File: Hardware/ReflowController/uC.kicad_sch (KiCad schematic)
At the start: 33 parts, among them J13 Conn_01x15_Female, J14 Conn_01x15_Female

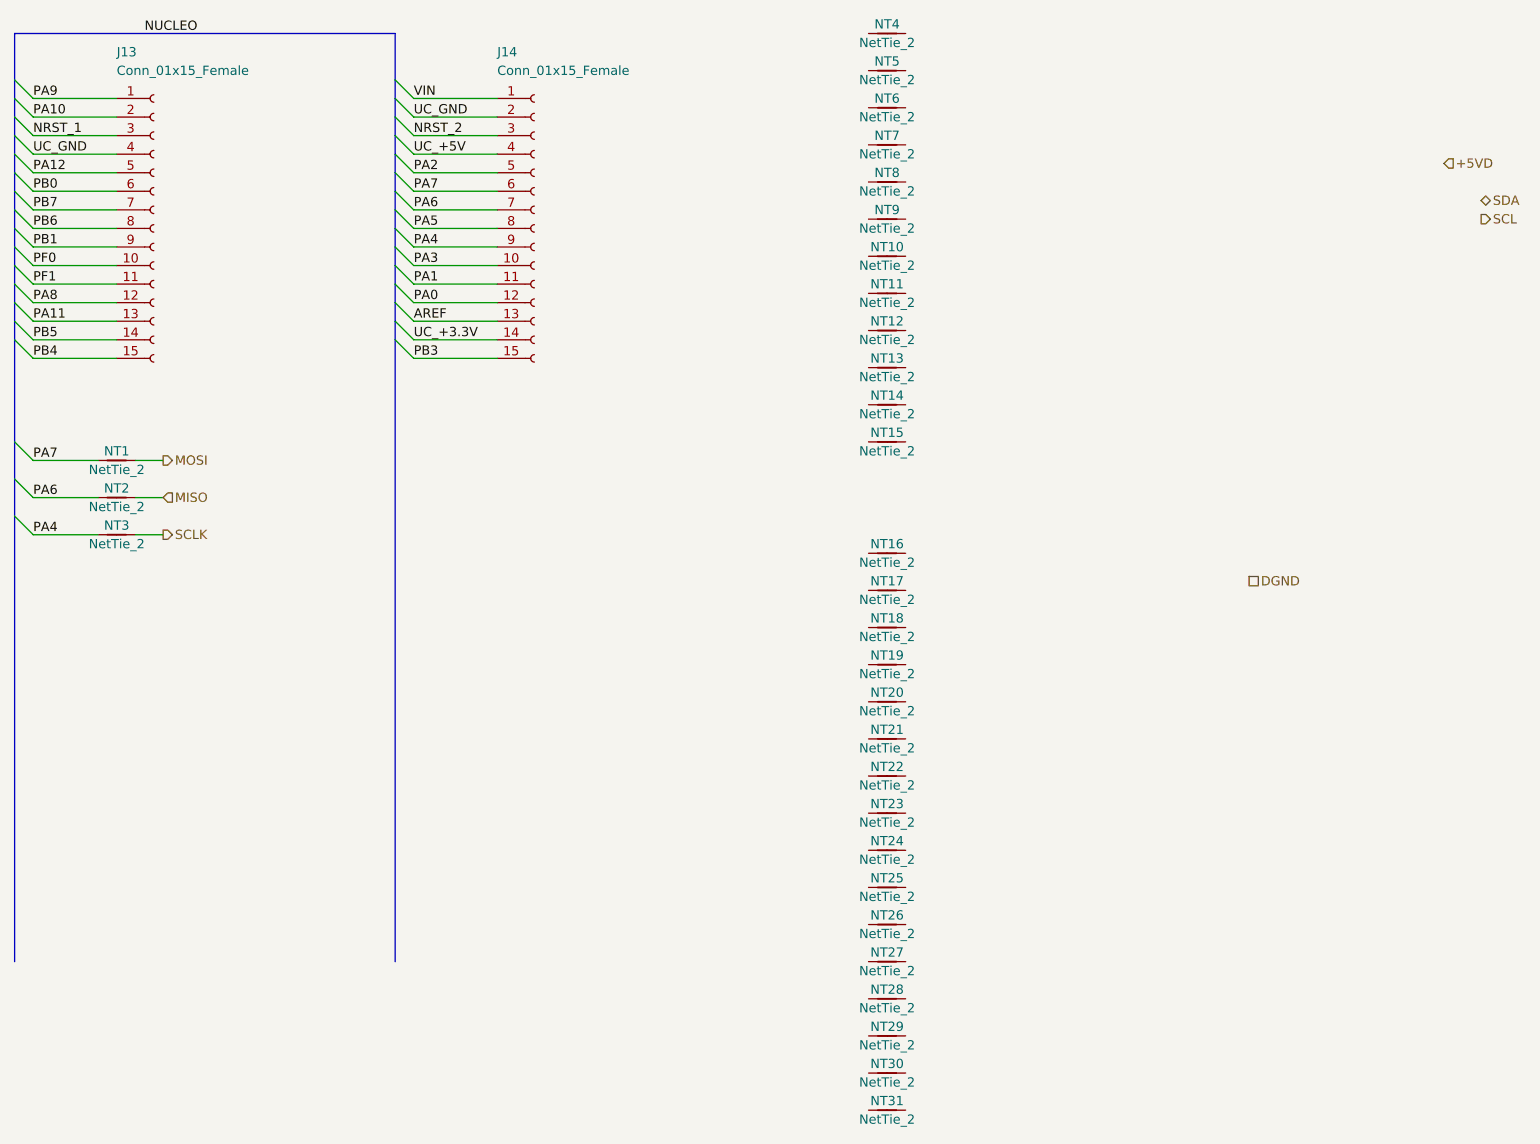
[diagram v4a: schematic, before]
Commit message: Finished the desing of the PSUand started with the PCB TODO: missing fuse find a solution
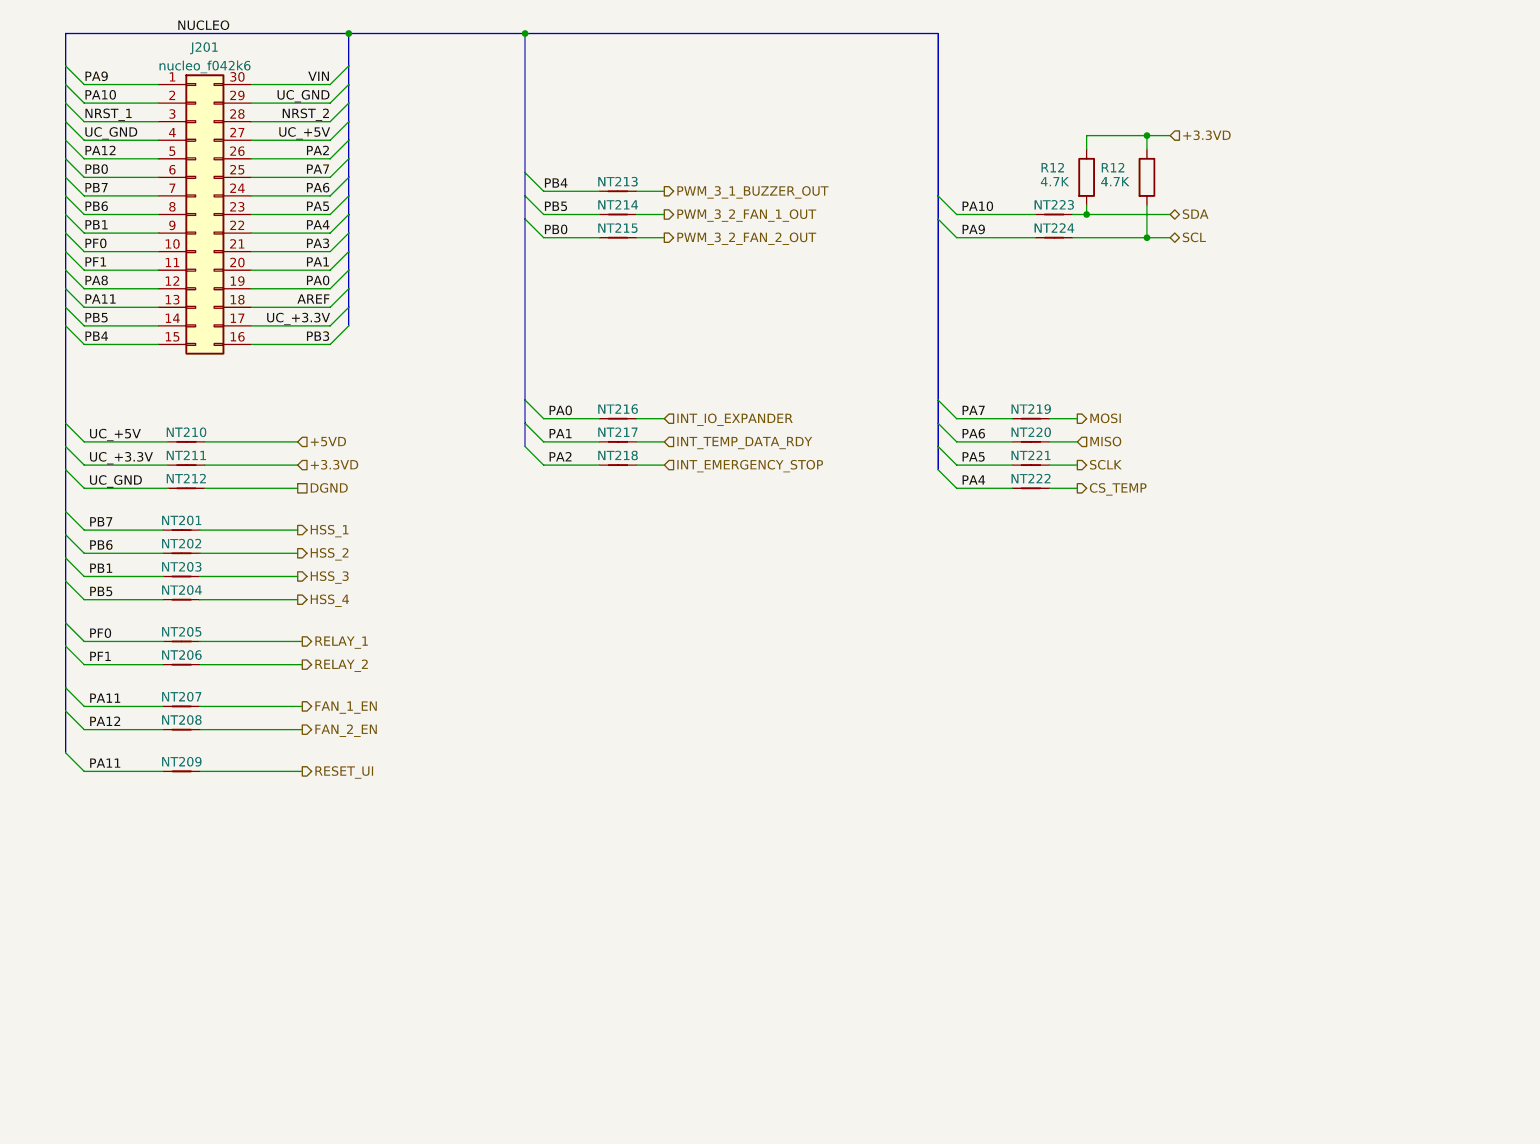
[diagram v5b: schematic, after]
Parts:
- removed J13, J14: Conn_01x15_Female, symbol Connector:Conn_01x15_Female
- removed NT1, NT10, NT11, NT12, NT13, NT14, NT15, NT16, NT17, NT18, NT19, NT2, NT20, NT21, NT22, NT23, NT24, NT25, NT26, NT27, NT28, NT29, NT3, NT30, NT31, NT4, NT5, NT6, NT7, NT8, NT9: NetTie_2, symbol Device:NetTie_2
- added J201: nucleo_f042k6, Module:Arduino_Nano, symbol Connector_Generic:Conn_02x15_Counter_Clockwise
- added NT201, NT202, NT203, NT204, NT205, NT206, NT207, NT208, NT209, NT210, NT211, NT212, NT213, NT214, NT215, NT216, NT217, NT218, NT219, NT220, NT221, NT222, NT223, NT224: NetTie_2, NetTie:NetTie-2_SMD_Pad0.5mm, symbol Device:NetTie_2
- added R12 (x2): 4.7K, Resistor_SMD:R_0603_1608Metric_Pad0.98x0.95mm_HandSolder, symbol Device:R
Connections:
- net +5VD: now also NT210.2
- net AREF: now also J201.18 (Pin_18)
- net DGND: now also NT212.2
- net MISO: now also NT220.2
- net MOSI: now also NT219.2
- net NRST_1: now also J201.3 (Pin_3)
- net NRST_2: now also J201.28 (Pin_28)
- net PA0: now also J201.19 (Pin_19), NT216.1
- net PA1: now also J201.20 (Pin_20), NT217.1
- net PA10: now also J201.2 (Pin_2), NT223.1
- net PA11: now also J201.13 (Pin_13), NT207.1, NT209.1
- net PA12: now also J201.5 (Pin_5), NT208.1
- net PA2: now also J201.26 (Pin_26), NT218.1
- net PA3: now also J201.21 (Pin_21)
- net PA4: now also J201.22 (Pin_22), NT222.1
- net PA5: now also J201.23 (Pin_23), NT221.1
- net PA6: now also J201.24 (Pin_24), NT220.1
- net PA7: now also J201.25 (Pin_25), NT219.1
- net PA8: now also J201.12 (Pin_12)
- net PA9: now also J201.1 (Pin_1), NT224.1
- net PB0: now also J201.6 (Pin_6), NT215.1
- net PB1: now also J201.9 (Pin_9), NT203.1
- net PB3: now also J201.16 (Pin_16)
- net PB4: now also J201.15 (Pin_15), NT213.1
- net PB5: now also J201.14 (Pin_14), NT204.1, NT214.1
- net PB6: now also J201.8 (Pin_8), NT202.1
- net PB7: now also J201.7 (Pin_7), NT201.1
- net PF0: now also J201.10 (Pin_10), NT205.1
- net PF1: now also J201.11 (Pin_11), NT206.1
- net SCL: now also NT224.2, R12.2
- net SCLK: now also NT221.2
- net SDA: now also NT223.2, R12.2
- net UC_+3.3V: now also J201.17 (Pin_17), NT211.1
- net UC_+5V: now also J201.27 (Pin_27), NT210.1
- net UC_GND: now also J201.29 (Pin_29), J201.4 (Pin_4), NT212.1
- net VIN: now also J201.30 (Pin_30)
- new net +3.3VD: NT211.2, R12.1, R12.1
- new net CS_TEMP: NT222.2
- new net FAN_1_EN: NT207.2
- new net FAN_2_EN: NT208.2
- new net HSS_1: NT201.2
- new net HSS_2: NT202.2
- new net HSS_3: NT203.2
- new net HSS_4: NT204.2
- new net INT_EMERGENCY_STOP: NT218.2
- new net INT_IO_EXPANDER: NT216.2
- new net INT_TEMP_DATA_RDY: NT217.2
- new net PWM_3_1_BUZZER_OUT: NT213.2
- new net PWM_3_2_FAN_1_OUT: NT214.2
- new net PWM_3_2_FAN_2_OUT: NT215.2
- new net RELAY_1: NT205.2
- new net RELAY_2: NT206.2
- new net RESET_UI: NT209.2

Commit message: Continuing on the PCB coorected some pins from the MCU
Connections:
- net PA11: no longer NT209.1
- net PA8: now also NT209.1
- net PB3: now also NT214.1
- net PB5: no longer NT214.1
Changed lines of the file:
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@@
+    (effects (font (size 1.27 1.27)) (justify left bottom))
+  )
+  (label "PB3" (at 97.79 50.165 0) (fields_autoplaced)
     (effects (font (size 1.27 1.27)) (justify left bottom))
   )
@@
   )
   (label "PA2" (at 98.425 84.455 0) (fields_autoplaced)
+    (effects (font (size 1.27 1.27)) (justify left bottom))
+  )
+  (label "PA8" (at 35.56 126.365 0) (fields_autoplaced)
     (effects (font (size 1.27 1.27)) (justify left bottom))
   )
@@
   (label "PA1" (at 68.58 57.785 180) (fields_autoplaced)
     (effects (font (size 1.27 1.27)) (justify right bottom))
-  )
-  (label "PA11" (at 35.56 126.365 0) (fields_autoplaced)
-    (effects (font (size 1.27 1.27)) (justify left bottom))
   )
   (label "NUCLEO" (at 47.625 25.4 0) (fields_autoplaced)
@@
     (effects (font (size 1.27 1.27)) (justify left bottom))
   )
-  (label "PB5" (at 97.79 50.165 0) (fields_autoplaced)
-    (effects (font (size 1.27 1.27)) (justify left bottom))
-  )

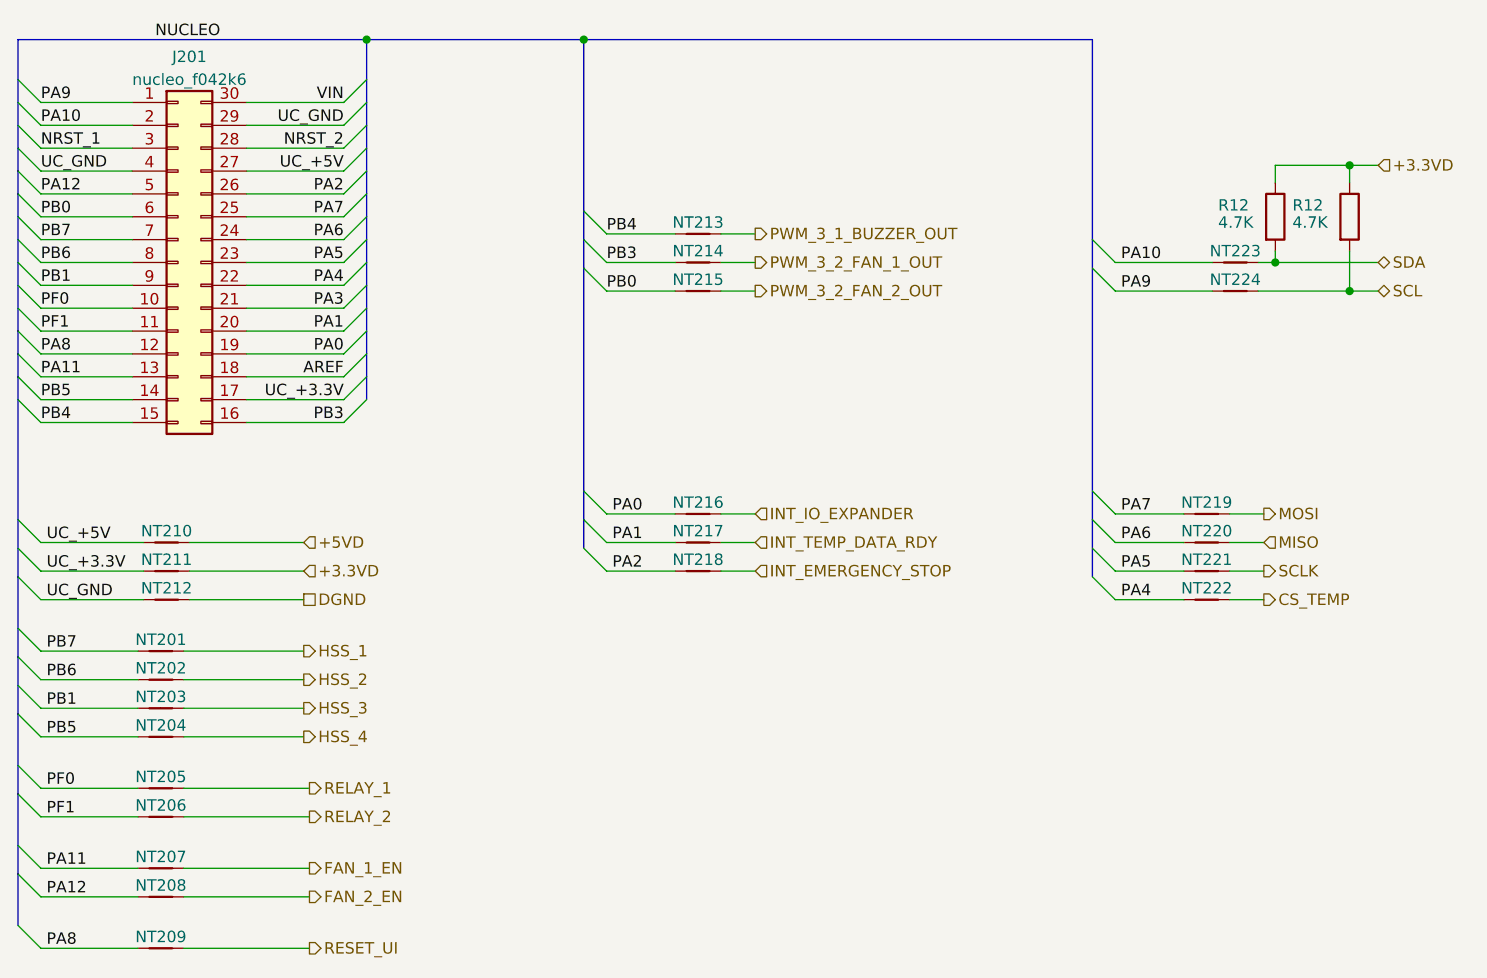
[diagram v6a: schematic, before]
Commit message: Advancing on the pcb removed netties from MCU
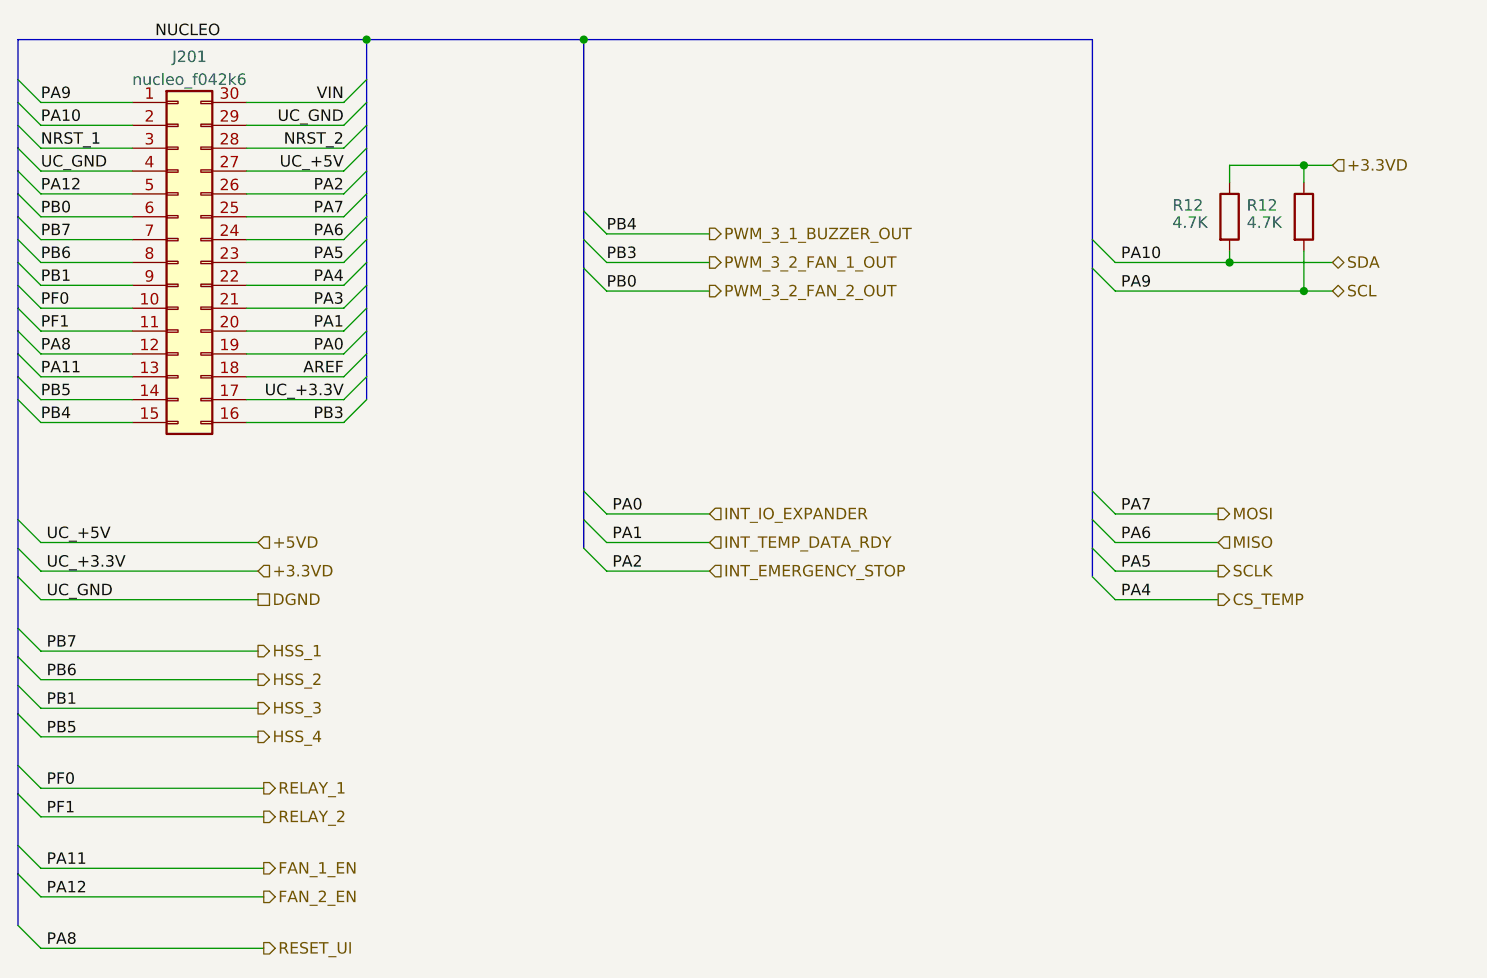
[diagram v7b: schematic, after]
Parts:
- removed NT201, NT202, NT203, NT204, NT205, NT206, NT207, NT208, NT209, NT210, NT211, NT212, NT213, NT214, NT215, NT216, NT217, NT218, NT219, NT220, NT221, NT222, NT223, NT224: NetTie_2, NetTie:NetTie-2_SMD_Pad0.5mm, symbol Device:NetTie_2
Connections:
- net PA0 is gone; now on net INT_IO_EXPANDER: J201.19 (Pin_19)
- net PA1 is gone; now on net INT_TEMP_DATA_RDY: J201.20 (Pin_20)
- net PA10 is gone; now on net SDA: J201.2 (Pin_2)
- net PA11 is gone; now on net FAN_1_EN: J201.13 (Pin_13)
- net PA12 is gone; now on net FAN_2_EN: J201.5 (Pin_5)
- net PA2 is gone; now on net INT_EMERGENCY_STOP: J201.26 (Pin_26)
- net PA4 is gone; now on net CS_TEMP: J201.22 (Pin_22)
- net PA5 is gone; now on net SCLK: J201.23 (Pin_23)
- net PA6 is gone; now on net MISO: J201.24 (Pin_24)
- net PA7 is gone; now on net MOSI: J201.25 (Pin_25)
- net PA8 is gone; now on net RESET_UI: J201.12 (Pin_12)
- net PA9 is gone; now on net SCL: J201.1 (Pin_1)
- net PB0 is gone; now on net PWM_3_2_FAN_2_OUT: J201.6 (Pin_6)
- net PB1 is gone; now on net HSS_3: J201.9 (Pin_9)
- net PB3 is gone; now on net PWM_3_2_FAN_1_OUT: J201.16 (Pin_16)
- net PB4 is gone; now on net PWM_3_1_BUZZER_OUT: J201.15 (Pin_15)
- net PB5 is gone; now on net HSS_4: J201.14 (Pin_14)
- net PB6 is gone; now on net HSS_2: J201.8 (Pin_8)
- net PB7 is gone; now on net HSS_1: J201.7 (Pin_7)
- net PF0 is gone; now on net RELAY_1: J201.10 (Pin_10)
- net PF1 is gone; now on net RELAY_2: J201.11 (Pin_11)
- net UC_+3.3V is gone; now on net +3.3VD: J201.17 (Pin_17)
- net UC_+5V is gone; now on net +5VD: J201.27 (Pin_27)
- net UC_GND is gone; now on net DGND: J201.29 (Pin_29), J201.4 (Pin_4)
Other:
- moved on the sheet: R12

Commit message: changed the uC schematic from the uC branch
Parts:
- removed J201: nucleo_f042k6, Module:Arduino_Nano, symbol Connector_Generic:Conn_02x15_Counter_Clockwise
- removed R12 (x2): 4.7K, Resistor_SMD:R_0603_1608Metric_Pad0.98x0.95mm_HandSolder, symbol Device:R
- added A1: NUCLEO_STM32F042K6, Module:Arduino_Nano, symbol MCU_Module:Arduino_Nano_v3.x
- added NT1, NT4, NT5, NT6, NT7: NetTie_2, symbol Device:NetTie_2
- added R2 (x2): 4k7, Resistor_SMD:R_1206_3216Metric, symbol Device:R
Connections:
- net +3.3VD: now also R2.1, R2.1
- net +5VD: now also A1.27 (+5V)
- net AREF: now also A1.18 (AREF)
- net DGND: now also A1.29 (GND), A1.4 (GND)
- net MISO: now also NT4.2
- net MOSI: now also NT1.2
- net PA3: now also A1.21 (A2)
- net SCL: now also NT7.2, R2.2
- net SCLK: now also NT5.2
- net SDA: now also NT6.2, R2.2
- new net PA0: A1.19 (A0)
- new net PA1: A1.20 (A1)
- new net PA10: A1.1 (D1/TX)
- new net PA11: A1.13 (D10)
- new net PA12: A1.5 (D2)
- new net PA2: A1.26 (A7)
- new net PA4: A1.22 (A3), NT5.1
- new net PA5: A1.23 (A4)
- new net PA6: A1.24 (A5), NT4.1
- new net PA7: A1.25 (A6), NT1.1
- new net PA8: A1.12 (D9)
- new net PA9: A1.2 (D0/RX)
- new net PB0: A1.6 (D3)
- new net PB1: A1.9 (D6)
- new net PB3: A1.16 (D13)
- new net PB4: A1.15 (D12)
- new net PB5: A1.14 (D11)
- new net PB6: A1.8 (D5), NT7.1
- new net PB7: A1.7 (D4), NT6.1
- new net PF0: A1.10 (D7)
- new net PF1: A1.11 (D8)
- new net ~{RESET}: A1.28 (~{RESET})
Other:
- note added: "I2C"
- note added: "NOTES"
- note added: "SPI"
- note added: "[1]"
- note added: "[1] : Please refer to the user manual UM1956 for further schematic information regarding the NUCLEO board"
- note added: "[2]"
- note added: "[2] : External 5V can be fed in while ST-Link also feeds the NUCLEO. The needed 3.3VD are generated on board from the 5VD."
